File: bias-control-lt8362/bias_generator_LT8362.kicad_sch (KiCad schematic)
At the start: 61 parts, among them IC1 LT8361EMSE/LT8362EMSE, IC2 ATSAMD21E18A-AF, IC4 MCP47FEB22A2-E_ST, J1 ISP, J2 Conn_01x04, J3 Conn_01x06, J4 USB_C_Receptacle_USB2.0_16P, U1 MIC5317-3.3YM5-TR, U2 RT9072B, U3 MCP6C02T-020E/CHY

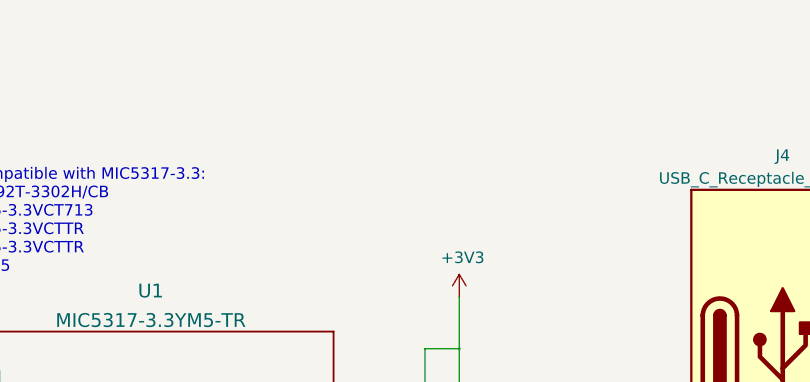
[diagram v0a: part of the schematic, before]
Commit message: Update KiCad designs for all 3 boards and re-export gerbers
- bias-control-lt8362: schematic + PCB updates, exported gerbers
  including new B_Paste/F_Paste layers
- power-supply: schematic + PCB updates, re-exported gerbers with new
  naming (.gbl/.gbs/.gto/.gtl/.gts) replacing old .gbr files, added
  paste layer exports
- tiav3_s14160: schematic + PCB updates, re-exported gerbers with new
  naming, added paste layer exports
- fp-lib-table updates across all four board projects
- new "w paste" gerber zip exports for assembly
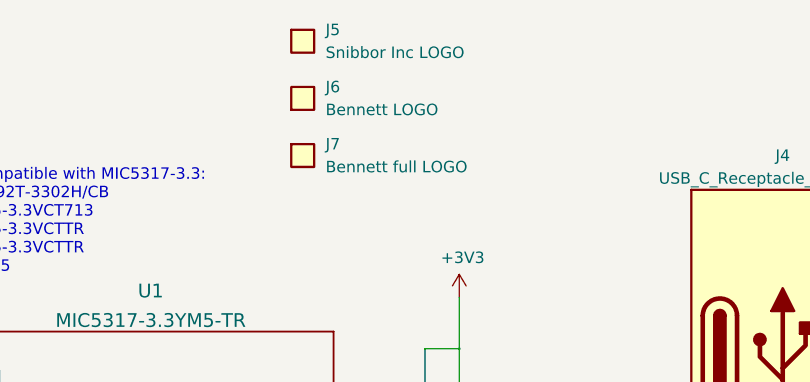
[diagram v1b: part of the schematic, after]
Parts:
- added J5: Snibbor Inc LOGO, snibbor_logos:snibbor_inc_logo, symbol Logo:Conn_NC
- added J6: Bennett LOGO, snibbor_logos:Bennett logo close 1 layered, symbol Logo:Conn_NC
- added J7: Bennett full LOGO, snibbor_logos:Bennett logo full 1 layered, symbol Logo:Conn_NC
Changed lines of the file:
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@@
 	)
 	(symbol
+		(lib_id "Logo:Conn_NC")
+		(at 77.47 24.13 90)
+		(unit 1)
+		(exclude_from_sim no)
+		(in_bom yes)
+		(on_board yes)
+		(dnp no)
+		(fields_autoplaced yes)
+		(property "Reference" "J6"
+			(at 80.01 22.8599 90)
+			(effects
+				(font
+					(size 1.27 1.27)
+				)
+				(justify right)
+			)
+		)
+		(property "Value" "Bennett LOGO"
+			(at 80.01 25.3999 90)
+			(effects
+				(font
+					(size 1.27 1.27)
+				)
+				(justify right)
+			)
+		)
+		(property "Footprint" "snibbor_logos:Bennett logo close 1 layered"
+			(at 77.47 24.13 0)
+			(effects
+				(font
+					(size 1.27 1.27)
+				)
+				(hide yes)
+			)
+		)
+		(property "Datasheet" ""
+			(at 77.47 24.13 0)
+			(effects
+				(font
+					(size 1.27 1.27)
+				)
+				(hide yes)
+			)
+		)
+		(property "Description" ""
+			(at 77.47 24.13 0)
+			(effects
+				(font
+					(size 1.27 1.27)
+				)
+				(hide yes)
+			)
+		)
+		(instances
+			(project "bias_generator_LT8362"
+				(path "/d66536fd-a221-45ef-b015-727e5772d2e0"
+					(reference "J6")
+					(unit 1)
+				)
+			)
+		)
+	)
+	(symbol
 		(lib_id "Device:C_Small")
 		(at 198.12 151.13 0)
@@
 	)
 	(symbol
+		(lib_id "Logo:Conn_NC")
+		(at 77.47 30.48 0)
+		(unit 1)
+		(exclude_from_sim no)
+		(in_bom yes)
+		(on_board yes)
+		(dnp no)
+		(fields_autoplaced yes)
+		(property "Reference" "J7"
+			(at 80.01 29.2099 0)
+			(effects
+				(font
+					(size 1.27 1.27)
+				)
+				(justify left)
+			)
+		)
+		(property "Value" "Bennett full LOGO"
+			(at 80.01 31.7499 0)
+			(effects
+				(font
+					(size 1.27 1.27)
+				)
+				(justify left)
+			)
+		)
+		(property "Footprint" "snibbor_logos:Bennett logo full 1 layered"
+			(at 77.47 30.48 0)
+			(effects
+				(font
+					(size 1.27 1.27)
+				)
+				(hide yes)
+			)
+		)
+		(property "Datasheet" ""
+			(at 77.47 30.48 0)
+			(effects
+				(font
+					(size 1.27 1.27)
+				)
+				(hide yes)
+			)
+		)
+		(property "Description" ""
+			(at 77.47 30.48 0)
+			(effects
+				(font
+					(size 1.27 1.27)
+				)
+				(hide yes)
+			)
+		)
+		(instances
+			(project "bias_generator_LT8362"
+				(path "/d66536fd-a221-45ef-b015-727e5772d2e0"
+					(reference "J7")
+					(unit 1)
+				)
+			)
+		)
+	)
+	(symbol
 		(lib_id "Device:C_Small")
 		(at 196.85 143.51 180)
@@
 					(unit 1)
 				)
+			)
+		)
+	)
+	(symbol
+		(lib_id "Logo:Conn_NC")
+		(at 77.47 17.78 0)
+		(unit 1)
+		(exclude_from_sim no)
+		(in_bom yes)
+		(on_board yes)
+		(dnp no)
+		(fields_autoplaced yes)
+		(property "Reference" "J5"
+			(at 80.01 16.5099 0)
+			(effects
+				(font
+					(size 1.27 1.27)
+				)
+				(justify left)
+			)
+		)
+		(property "Value" "Snibbor Inc LOGO"
+			(at 80.01 19.0499 0)
+			(effects
+				(font
+					(size 1.27 1.27)
+				)
+				(justify left)
+			)
+		)
+		(property "Footprint" "snibbor_logos:snibbor_inc_logo"
+			(at 77.47 17.78 0)
+			(effects
+				(font
+					(size 1.27 1.27)
+				)
+				(hide yes)
+			)
+		)
+		(property "Datasheet" ""
+			(at 77.47 17.78 0)
+			(effects
+				(font
+					(size 1.27 1.27)
+				)
+				(hide yes)
+			)
+		)
+		(property "Description" ""
+			(at 77.47 17.78 0)
+			(effects
+				(font
+					(size 1.27 1.27)
+				)
+				(hide yes)
+			)
+		)
+		(instances
+			(project ""
+				(path "/d66536fd-a221-45ef-b015-727e5772d2e0"
+					(reference "J5")
+					(unit 1)
+				)

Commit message: sourcing, ordering, and assembling
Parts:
- U2: value RT9072B -> RT9072B(ob)/LT3014ES5#TRP
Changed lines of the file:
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@@
 		(on_board yes)
 		(dnp no)
-		(fields_autoplaced yes)
 		(property "Reference" "U2"
 			(at 178.435 139.5942 0)
@@
 			)
 		)
-		(property "Value" "RT9072B"
-			(at 178.435 142.3693 0)
+		(property "Value" "RT9072B(ob)/LT3014ES5#TRP"
+			(at 173.736 162.052 0)
 			(effects
 				(font
